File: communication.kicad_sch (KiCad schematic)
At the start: 3 parts, among them U501 MAX3078E

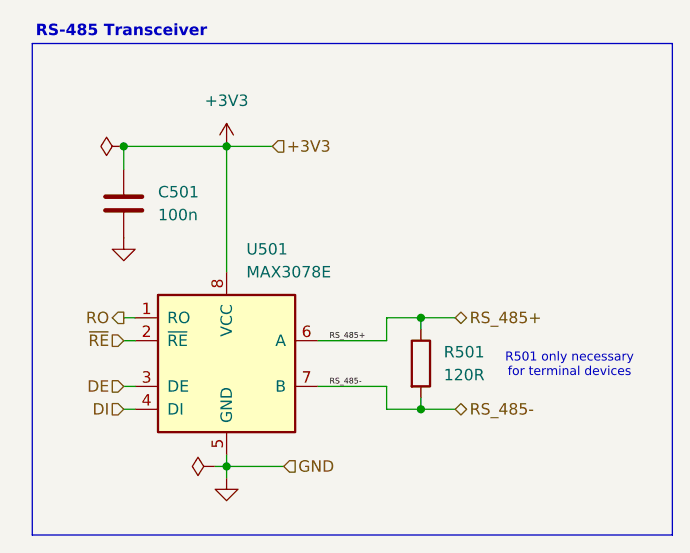
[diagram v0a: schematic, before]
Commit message: Changed motor power supply
Removed 5V power rail. Migrated 3.3V rail to TPS62160
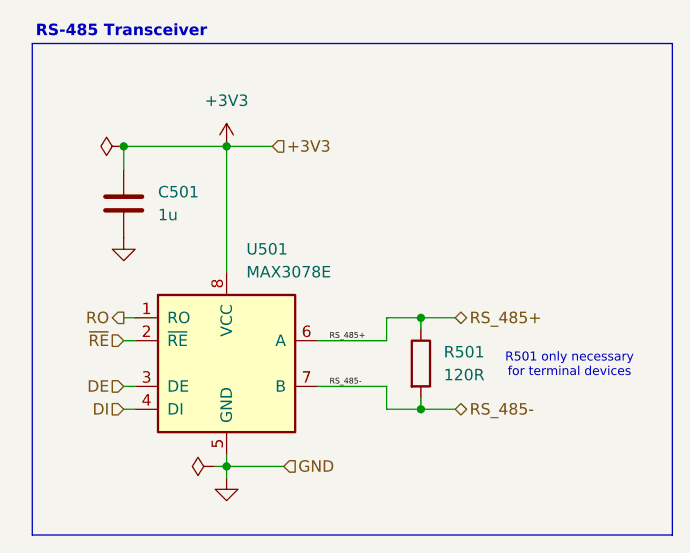
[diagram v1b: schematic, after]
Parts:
- C501: value 100n -> 1u; footprint (none) -> Capacitor_SMD:C_0603_1608Metric
- R501: footprint (none) -> Resistor_SMD:R_0603_1608Metric
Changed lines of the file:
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@@
 		(dnp no)
 		(fields_autoplaced yes)
-		(property "Reference" "#PWR0503"
+		(property "Reference" "#PWR0502"
 			(at 139.7 83.82 0)
 			(effects
@@
 			(project "Vacuum_Tweezers"
 				(path "/25b5e35e-9397-4bb5-a91c-fc11ba49a08d/54a5654d-3f03-4847-a65f-052fca6082a9"
-					(reference "#PWR0503")
+					(reference "#PWR0502")
 					(unit 1)
 				)
@@
 			)
 		)
-		(property "Value" "100n"
+		(property "Value" "1u"
 			(at 132.08 87.6299 0)
 			(effects
@@
 			)
 		)
-		(property "Footprint" ""
+		(property "Footprint" "Capacitor_SMD:C_0603_1608Metric"
 			(at 129.2352 90.17 0)
 			(effects
@@
 			)
 		)
-		(property "Footprint" ""
+		(property "Footprint" "Resistor_SMD:R_0603_1608Metric"
 			(at 159.512 104.14 90)
 			(effects
@@
 		(dnp no)
 		(fields_autoplaced yes)
-		(property "Reference" "#PWR0502"
+		(property "Reference" "#PWR0503"
 			(at 139.7 123.19 0)
 			(effects
@@
 			(project "Vacuum_Tweezers"
 				(path "/25b5e35e-9397-4bb5-a91c-fc11ba49a08d/54a5654d-3f03-4847-a65f-052fca6082a9"
-					(reference "#PWR0502")
-					(unit 1)
-				)
+					(reference "#PWR0503")
+					(unit 1)
+				)
